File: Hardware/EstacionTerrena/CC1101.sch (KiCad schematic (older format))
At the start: 19 parts, among them U4 CC1101RGP, U5 0915BM15A0001E, Y2 26 MHz

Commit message: Corrección de librerías en PCB de estación terrena
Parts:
- removed U4: CC1101RGP, SamacSys_Parts:QFN50P400X400X100-21N-D, symbol EstacionTerrena-rescue:CC1101RGP-SamacSys_Parts
- removed U5: 0915BM15A0001E, SamacSys_Parts:0915BM15A0001E, symbol EstacionTerrena-rescue:0915BM15A0001E-SamacSys_Parts
- added U4: CC1101RGP, QFN50P400X400X100-21N-D, symbol SamacSys_Parts:CC1101RGP
- added U5: 0915BM15A0001E, 0915BM15A0001E, symbol SamacSys_Parts:0915BM15A0001E
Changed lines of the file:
@@
 EESchema Schematic File Version 4
 LIBS:EstacionTerrena-cache
-EELAYER 26 0
+EELAYER 29 0
 EELAYER END
 $Descr A4 11693 8268
@@
 	0    -1   -1   0
 $EndComp
-$Comp
-L EstacionTerrena-rescue:0915BM15A0001E-SamacSys_Parts U5
-U 1 1 5BF115E1
-P 7150 3400
-F 0 "U5" H 7150 3766 50  0000 C CNN
-F 1 "0915BM15A0001E" H 7150 3674 50  0000 C CNN
-F 2 "SamacSys_Parts:0915BM15A0001E" H 7500 3600 50  0001 L CNN
-F 3 "http://www.mouser.com/datasheet/2/611/0915BM15A0001-242333.pdf" H 7500 3500 50  0001 L CNN
-F 4 "Signal Conditioning 915MHz BALUN/FILTER" H 7500 3400 50  0001 L CNN "Description"
-F 5 "0.8" H 7500 3300 50  0001 L CNN "Height"
-F 6 "JOHANSON TECHNOLOGY" H 7500 3200 50  0001 L CNN "Manufacturer_Name"
-F 7 "0915BM15A0001E" H 7500 3100 50  0001 L CNN "Manufacturer Part Number"
-F 8 "0915BM15A0001E" H 7500 3000 50  0001 L CNN "Arrow Part Number"
-	1    7150 3400
-	1    0    0    -1
-$EndComp
 Wire Wire Line
 	6400 3300 6650 3300
@@
 Wire Wire Line
 	2900 2300 3500 2300
-$Comp
-L EstacionTerrena-rescue:CC1101RGP-SamacSys_Parts U4
-U 1 1 5BBFFFB0
-P 2900 3150
-F 0 "U4" H 4200 3800 50  0000 L CNN
-F 1 "CC1101RGP" H 4200 3700 50  0000 L CNN
-F 2 "SamacSys_Parts:QFN50P400X400X100-21N-D" H 4250 3650 50  0001 L CNN
-F 3 "http://www.ti.com/lit/ds/symlink/cc1101.pdf" H 4250 3550 50  0001 L CNN
-F 4 "Texas Instruments CC1101RGP, RF Transceiver IC Triple Band 1.8  3.6 V 20-Pin QFN" H 4250 3450 50  0001 L CNN "Description"
-F 5 "1" H 4250 3350 50  0001 L CNN "Height"
-F 6 "Texas Instruments" H 4250 3250 50  0001 L CNN "Manufacturer_Name"
-F 7 "CC1101RGP" H 4250 3150 50  0001 L CNN "Manufacturer Part Number"
-F 8 "8203068P" H 4250 3050 50  0001 L CNN "RS Part Number"
-F 9 "http://uk.rs-online.com/web/p/products/8203068P" H 4250 2950 50  0001 L CNN "RS Price/Stock"
-F 10 "CC1101RGP" H 4250 2850 50  0001 L CNN "Arrow Part Number"
-F 11 "https://www.arrow.com/en/products/cc1101rgp/texas-instruments" H 4250 2750 50  0001 L CNN "Arrow Price/Stock"
-	1    2900 3150
-	1    0    0    -1
-$EndComp
 Text HLabel 3150 4700 0    50   Input ~ 0
 CS
@@
 F 6 "GCM155R71C104KA55D" H 4500 3750 50  0001 C CNN "Manufacturer Part Number"
 	1    4500 3750
-	-1   0    0    -1
+	1    0    0    -1
 $EndComp
 $Comp
@@
 EndData
 $EndBitmap
+$Comp
+L SamacSys_Parts:CC1101RGP U4
+U 1 1 5CD02CD0
+P 2900 3150
+F 0 "U4" H 4000 3850 50  0000 L CNN
+F 1 "CC1101RGP" H 4000 3750 50  0000 L CNN
+F 2 "QFN50P400X400X100-21N-D" H 4250 3650 50  0001 L CNN
+F 3 "http://www.ti.com/lit/ds/symlink/cc1101.pdf" H 4250 3550 50  0001 L CNN
+F 4 "Texas Instruments CC1101RGP, RF Transceiver IC Triple Band 1.8  3.6 V 20-Pin QFN" H 4250 3450 50  0001 L CNN "Description"
+F 5 "1" H 4250 3350 50  0001 L CNN "Height"
+F 6 "Texas Instruments" H 4250 3250 50  0001 L CNN "Manufacturer_Name"
+F 7 "CC1101RGP" H 4250 3150 50  0001 L CNN "Manufacturer Part Number"
+F 8 "8203068P" H 4250 3050 50  0001 L CNN "RS Part Number"
+F 9 "http://uk.rs-online.com/web/p/products/8203068P" H 4250 2950 50  0001 L CNN "RS Price/Stock"
+F 10 "CC1101RGP" H 4250 2850 50  0001 L CNN "Arrow Part Number"
+F 11 "https://www.arrow.com/en/products/cc1101rgp/texas-instruments" H 4250 2750 50  0001 L CNN "Arrow Price/Stock"
+	1    2900 3150
+	1    0    0    -1
+$EndComp
+$Comp
+L SamacSys_Parts:0915BM15A0001E U5
+U 1 1 5CD0A297
+P 7150 3400
+F 0 "U5" H 7150 3765 50  0000 C CNN
+F 1 "0915BM15A0001E" H 7150 3674 50  0000 C CNN
+F 2 "0915BM15A0001E" H 7500 3600 50  0001 L CNN
+F 3 "http://www.mouser.com/datasheet/2/611/0915BM15A0001-242333.pdf" H 7500 3500 50  0001 L CNN
+F 4 "Signal Conditioning 915MHz BALUN/FILTER" H 7500 3400 50  0001 L CNN "Description"
+F 5 "0.8" H 7500 3300 50  0001 L CNN "Height"
+F 6 "JOHANSON TECHNOLOGY" H 7500 3200 50  0001 L CNN "Manufacturer_Name"
+F 7 "0915BM15A0001E" H 7500 3100 50  0001 L CNN "Manufacturer Part Number"
+F 8 "0915BM15A0001E" H 7500 3000 50  0001 L CNN "Arrow Part Number"
+	1    7150 3400
+	1    0    0    -1
+$EndComp
 $EndSCHEMATC

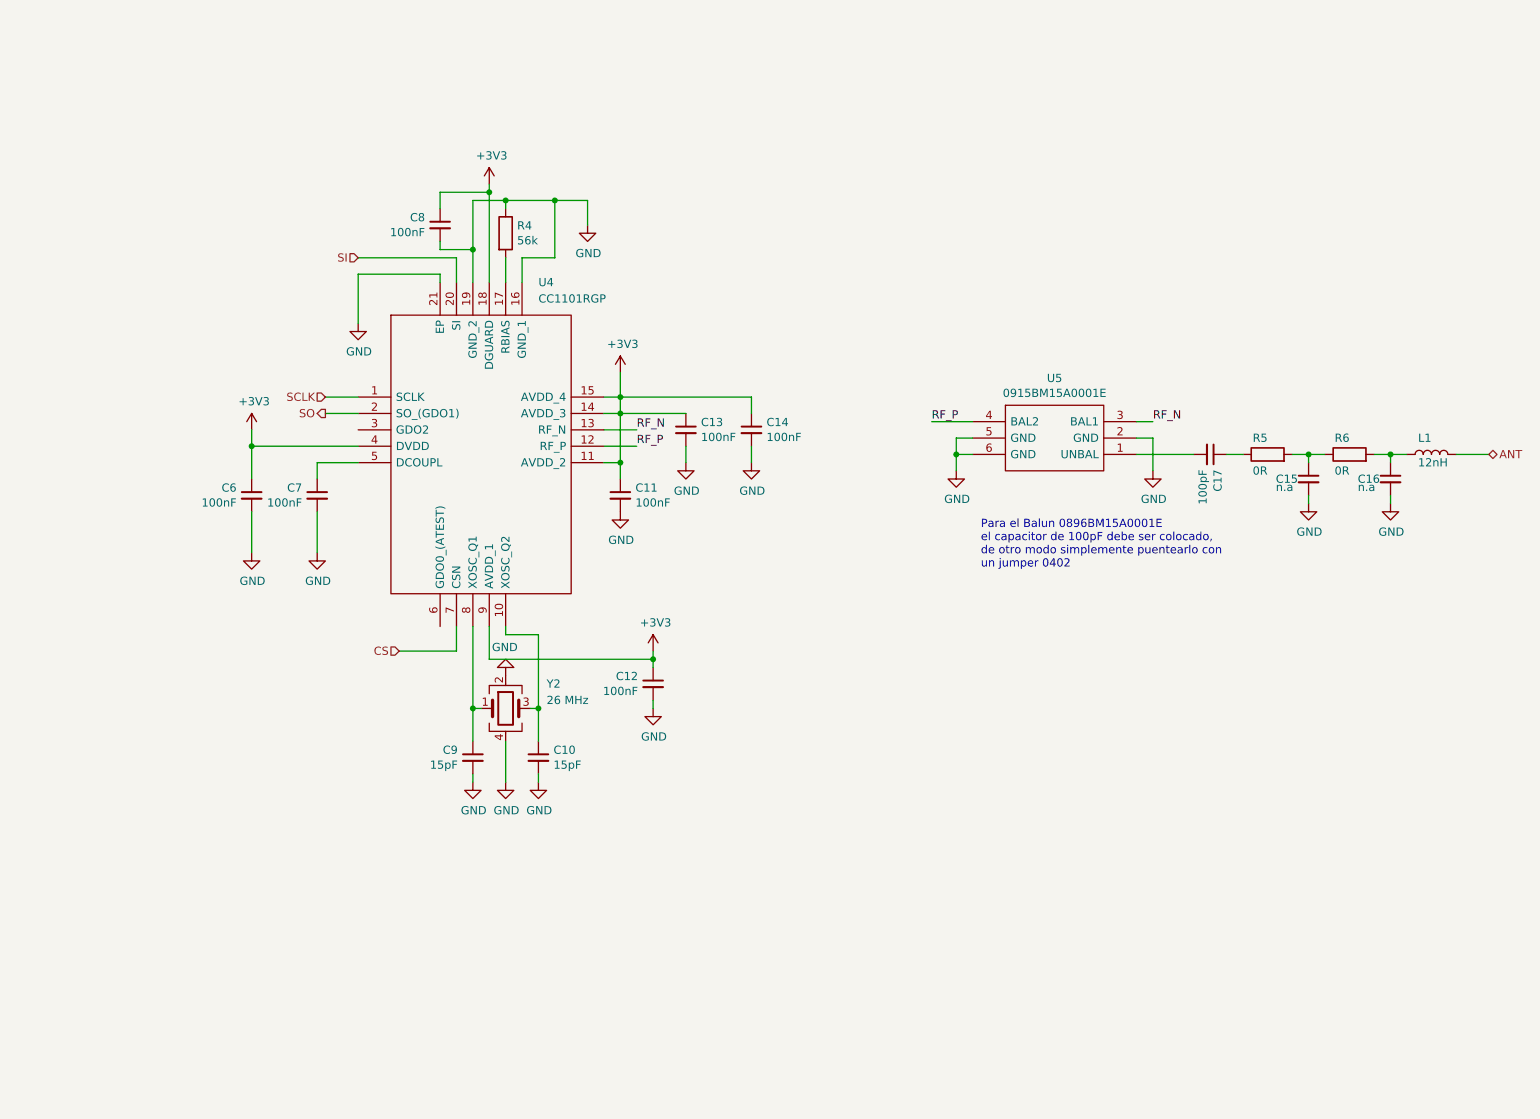
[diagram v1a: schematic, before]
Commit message: Agregado CC1190 a estación terrena
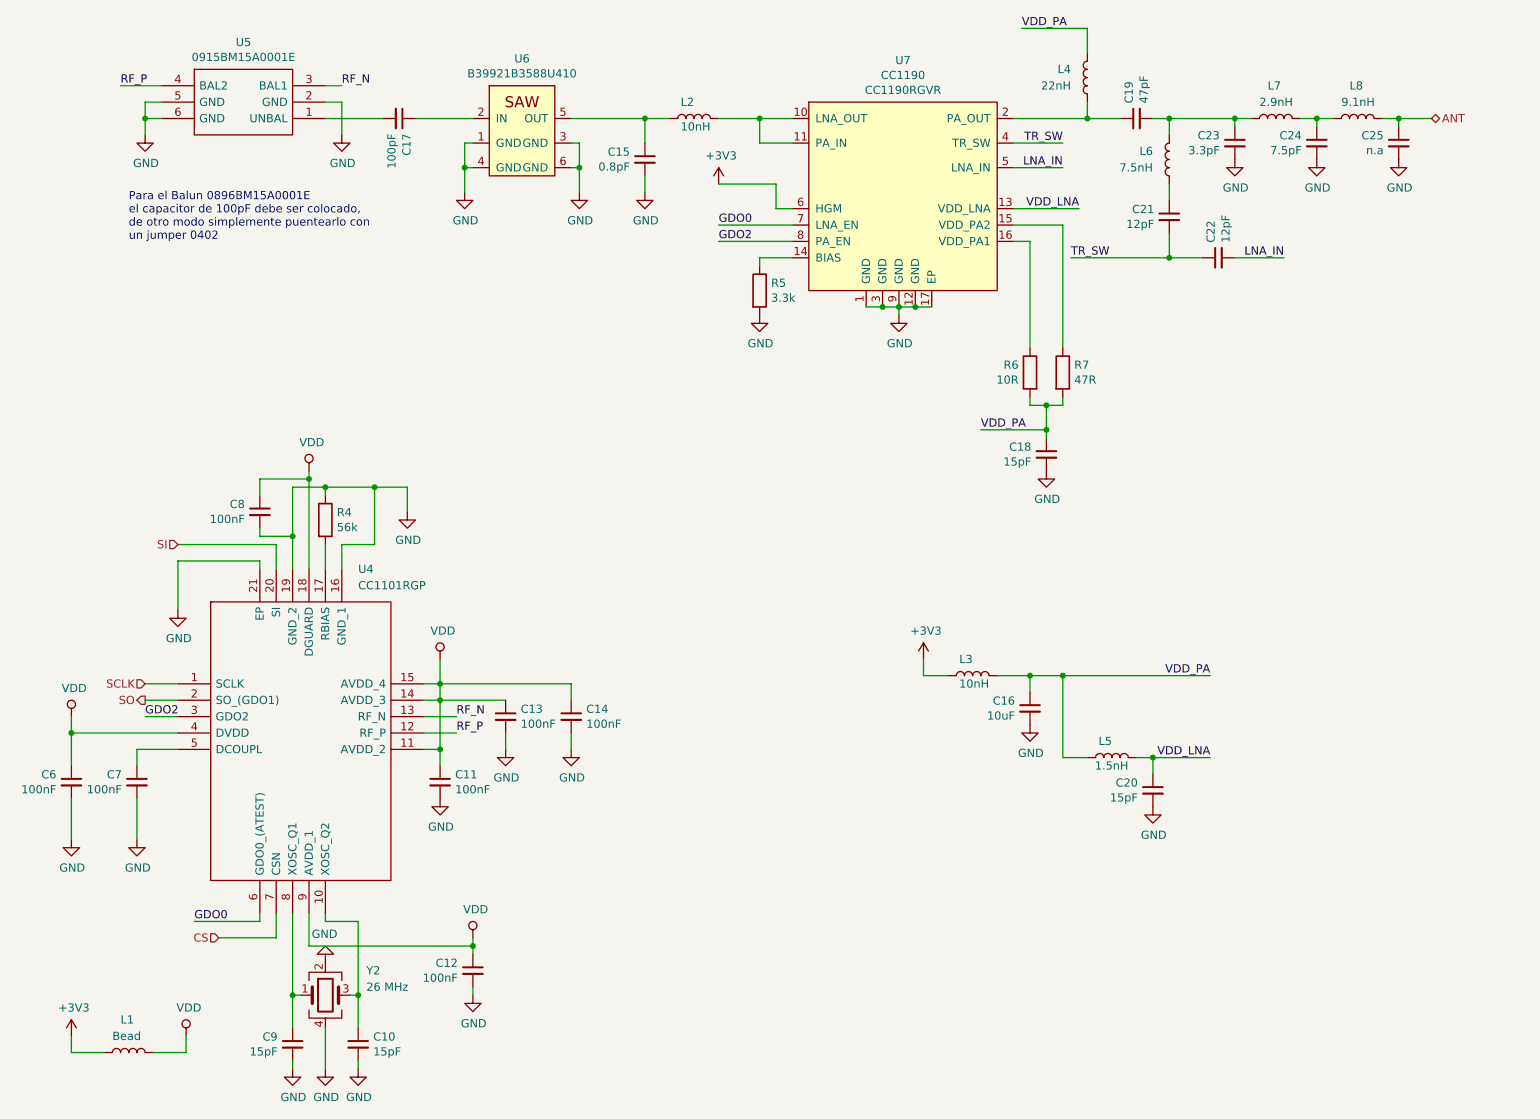
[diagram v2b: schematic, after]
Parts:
- added C18, C20: 15pF, Capacitor_SMD:C_0402_1005Metric, symbol Device:C_Small
- added C19: 47pF, Capacitor_SMD:C_0402_1005Metric, symbol Device:C_Small
- added C21, C22: 12pF, Capacitor_SMD:C_0402_1005Metric, symbol Device:C_Small
- added C23: 3.3pF, Capacitor_SMD:C_0402_1005Metric, symbol Device:C_Small
- added C24: 7.5pF, Capacitor_SMD:C_0402_1005Metric, symbol Device:C_Small
- added C25: n.a, Capacitor_SMD:C_0402_1005Metric, symbol Device:C_Small
- added L2, L3: 10nH, Inductor_SMD:L_0402_1005Metric, symbol Device:L
- added L4: 22nH, Inductor_SMD:L_0603_1608Metric_Pad1.05x0.95mm_HandSolder, symbol Device:L
- added L5: 1.5nH, Inductor_SMD:L_0402_1005Metric, symbol Device:L
- added L6: 7.5nH, Inductor_SMD:L_0402_1005Metric, symbol Device:L
- added L7: 2.9nH, Inductor_SMD:L_0402_1005Metric, symbol Device:L
- added L8: 9.1nH, Inductor_SMD:L_0402_1005Metric, symbol Device:L
- added R7: 47R, Resistor_SMD:R_0402_1005Metric, symbol Device:R
- added U6: B39921B3588U410, AXTEC:B39921B3588U410, symbol AXTEC_IC:B39921B3588U410
- added U7: CC1190, Package_DFN_QFN:Texas_S-PVQFN-N16_EP2.7x2.7mm, symbol AXTEC_IC:CC1190
- C15: value n.a -> 0.8pF; Dielectric (none) -> NP0; Manufacturer Part Number (none) -> GRM1555C2AR80BA01D
- C16: value n.a -> 10uF; footprint Capacitor_SMD:C_0402_1005Metric -> Capacitor_SMD:C_0805_2012Metric_Pad1.15x1.40mm_HandSolder; Dielectric (none) -> NP0; Manufacturer Part Number (none) -> C2012X7R1A106M125AC
- L1: value 12nH -> Bead; Manufacturer Part Number L-07C12NJV6 -> BLM15HG102SN1D
- R5: value 0R -> 3.3k; Manufacturer Part Number RC0402JR-070RL -> RC0402FR-073K3L
- R6: value 0R -> 10R; Manufacturer Part Number RC0402JR-070RL -> RC0402FR-0710RL
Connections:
- net +3V3: now also L1.2, L3.1, U7.6 (HGM); no longer C11.1, C12.1, C13.1, C14.1, C6.1, C8.1, U4.11 (AVDD_2), U4.14 (AVDD_3), U4.15 (AVDD_4), U4.18 (DGUARD), U4.4 (DVDD), U4.9 (AVDD_1)
- net ANT: now also C25.1, L8.1; no longer L1.2
- net GND: now also R5.2, C18.2, C20.2, C23.2, C24.2, C25.2, U6.1 (GND), U6.3 (GND), U6.4 (GND), U6.6 (GND), U7.1 (GND), U7.12 (GND), U7.17 (EP), U7.3 (GND), U7.9 (GND)
- net at C17.1: now also U6.2 (IN); no longer R5.1
- net VDD_PA: now reaches C16.1, R6.2
- net VDD_PA: now also C18.1, L3.2, L4.1, L5.1, R7.2; no longer L1.1
- net GDO2: now reaches U4.3 (GDO2)
- net GDO2: now also U7.8 (PA_EN)
- net GDO0: now reaches U4.6 (GDO0_(ATEST))
- net GDO0: now also U7.7 (LNA_EN)
- new net: C15.1, L2.1, U6.5 (OUT)
- new net: L2.2, U7.10 (LNA_OUT), U7.11 (PA_IN)
- new net: C19.1, L4.2, U7.2 (PA_OUT)
- new net: C19.2, C23.1, L6.1, L7.2
- new net: C21.1, L6.2
- new net: C24.1, L7.1, L8.2
- new net: R5.1, U7.14 (BIAS)
- new net: R7.1, U7.15 (VDD_PA2)
- new net: R6.1, U7.16 (VDD_PA1)
- new net LNA_IN: C22.2, U7.5 (LNA_IN)
- new net TR_SW: C21.2, C22.1, U7.4 (TR_SW)
- new net VDD: C11.1, C12.1, C13.1, C14.1, C6.1, C8.1, L1.1, U4.11 (AVDD_2), U4.14 (AVDD_3), U4.15 (AVDD_4), U4.18 (DGUARD), U4.4 (DVDD), U4.9 (AVDD_1)
- new net VDD_LNA: C20.1, L5.2, U7.13 (VDD_LNA)
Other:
- moved on the sheet: C10, C11, C12, C13, C14, C17, C6, C7, C8, C9, R4, U4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

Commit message: Estacion terrena:
- Nuevo LDO de 500mA para poder utilizar el CC1190 a toda su potencia de ser necesario
- Cambiado el MCP2210 por un PIC18F14K50 ya que el MCP2210 es MUY lento para transferencias SPI
- Agregado de footprints faltantes
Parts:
- U4: footprint QFN50P400X400X100-21N-D -> Package_DFN_QFN:QFN-20-1EP_4x4mm_P0.5mm_EP2.5x2.5mm
- U5: footprint 0915BM15A0001E -> SamacSys_Parts:0915BM15A0001E
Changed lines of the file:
@@
 F 0 "U4" H 2900 5600 50  0000 L CNN
 F 1 "CC1101RGP" H 2900 5500 50  0000 L CNN
-F 2 "QFN50P400X400X100-21N-D" H 3150 5400 50  0001 L CNN
+F 2 "Package_DFN_QFN:QFN-20-1EP_4x4mm_P0.5mm_EP2.5x2.5mm" H 3150 5400 50  0001 L CNN
 F 3 "http://www.ti.com/lit/ds/symlink/cc1101.pdf" H 3150 5300 50  0001 L CNN
 F 4 "Texas Instruments CC1101RGP, RF Transceiver IC Triple Band 1.8  3.6 V 20-Pin QFN" H 3150 5200 50  0001 L CNN "Description"
@@
 F 0 "U5" H 2200 1715 50  0000 C CNN
 F 1 "0915BM15A0001E" H 2200 1624 50  0000 C CNN
-F 2 "0915BM15A0001E" H 2550 1550 50  0001 L CNN
+F 2 "SamacSys_Parts:0915BM15A0001E" H 2550 1550 50  0001 L CNN
 F 3 "http://www.mouser.com/datasheet/2/611/0915BM15A0001-242333.pdf" H 2550 1450 50  0001 L CNN
 F 4 "Signal Conditioning 915MHz BALUN/FILTER" H 2550 1350 50  0001 L CNN "Description"

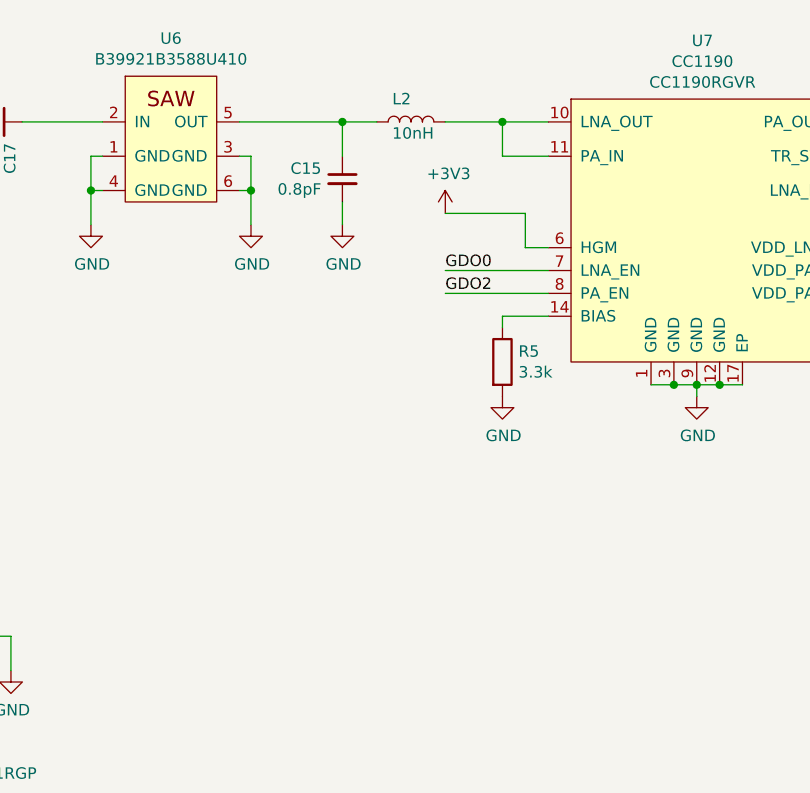
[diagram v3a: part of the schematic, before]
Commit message: Agregado jumper de selección de ganancia para CC1190 en ET
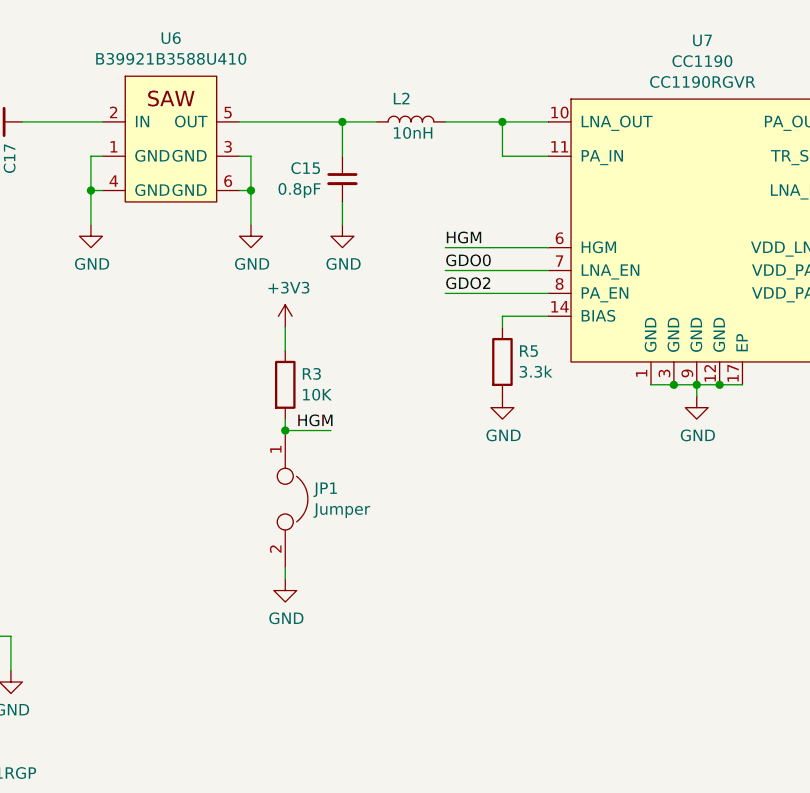
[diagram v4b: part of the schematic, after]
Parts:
- added JP1: Jumper, Jumper:SolderJumper-2_P1.3mm_Open_RoundedPad1.0x1.5mm, symbol Device:Jumper
- added R3: 10K, Resistor_SMD:R_0603_1608Metric_Pad1.05x0.95mm_HandSolder, symbol Device:R
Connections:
- net +3V3: now also R3.1; no longer U7.6 (HGM)
- net GND: now also JP1.2
- new net HGM: JP1.1, R3.2, U7.6 (HGM)
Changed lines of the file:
@@
 	5550 2100 5100 2100
-Wire Wire Line
-	5100 1850 5450 1850
-Wire Wire Line
-	5450 2000 5450 1850
-Wire Wire Line
-	5550 2000 5450 2000
 Wire Wire Line
 	5350 1450 5550 1450
@@
 RF_N
 $Comp
-L power:+3V3 #PWR033
-U 1 1 5CCF98DA
-P 5100 1850
-F 0 "#PWR033" H 5100 1700 50  0001 C CNN
-F 1 "+3V3" H 5115 2023 50  0000 C CNN
-F 2 "" H 5100 1850 50  0001 C CNN
-F 3 "" H 5100 1850 50  0001 C CNN
-	1    5100 1850
-	1    0    0    -1
-$EndComp
-$Comp
 L power:+3V3 #PWR049
 U 1 1 5CCFCB92
@@
 	1    0    0    -1
 $EndComp
+$Comp
+L power:GND #PWR016
+U 1 1 5CD4AF72
+P 4400 3450
+AR Path="/5B9A8077/5CD4AF72" Ref="#PWR016"  Part="1"
+AR Path="/5BA17F9C/5CD4AF72" Ref="#PWR?"  Part="1"
+F 0 "#PWR016" H 4400 3200 50  0001 C CNN
+F 1 "GND" H 4405 3277 50  0000 C CNN
+F 2 "" H 4400 3450 50  0001 C CNN
+F 3 "" H 4400 3450 50  0001 C CNN
+	1    4400 3450
+	1    0    0    -1
+$EndComp
+$Comp
+L Device:R R3
+U 1 1 5CD6637D
+P 4400 2600
+AR Path="/5B9A8077/5CD6637D" Ref="R3"  Part="1"
+AR Path="/5BA17F9C/5CD6637D" Ref="R?"  Part="1"
+F 0 "R3" H 4470 2646 50  0000 L CNN
+F 1 "10K" H 4470 2555 50  0000 L CNN
+F 2 "Resistor_SMD:R_0603_1608Metric_Pad1.05x0.95mm_HandSolder" V 4330 2600 50  0001 C CNN
+F 3 "~" H 4400 2600 50  0001 C CNN
+F 4 "RC0603JR-0710KL" H 4400 2600 50  0001 C CNN "Manufacturer Part Number"
+	1    4400 2600
+	1    0    0    -1
+$EndComp
+Wire Wire Line
+	5550 2000 5100 2000
+Text Label 5100 2000 0    50   ~ 0
+HGM
+Text Label 4450 2800 0    50   ~ 0
+HGM
+$Comp
+L power:+3V3 #PWR015
+U 1 1 5CDA2E4F
+P 4400 2350
+F 0 "#PWR015" H 4400 2200 50  0001 C CNN
+F 1 "+3V3" H 4415 2523 50  0000 C CNN
+F 2 "" H 4400 2350 50  0001 C CNN
+F 3 "" H 4400 2350 50  0001 C CNN
+	1    4400 2350
+	1    0    0    -1
+$EndComp
+Wire Wire Line
+	4400 2350 4400 2450
+$Comp
+L Device:Jumper JP1
+U 1 1 5CD5F03C
+P 4400 3100
+F 0 "JP1" V 4354 3227 50  0000 L CNN
+F 1 "Jumper" V 4445 3227 50  0000 L CNN
+F 2 "Jumper:SolderJumper-2_P1.3mm_Open_RoundedPad1.0x1.5mm" H 4400 3100 50  0001 C CNN
+F 3 "~" H 4400 3100 50  0001 C CNN
+	1    4400 3100
+	0    1    1    0
+$EndComp
+Wire Wire Line
+	4400 2750 4400 2800
+Wire Wire Line
+	4400 3400 4400 3450
+Wire Wire Line
+	4400 2800 4600 2800
+Connection ~ 4400 2800
 $EndSCHEMATC

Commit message: Estación terrena BOM
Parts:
- U7: Manufactuer Part Number CC1190RGVR -> (none); Manufacturer Part Number (none) -> CC1190RGVR
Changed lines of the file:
@@
 F 2 "Package_DFN_QFN:Texas_S-PVQFN-N16_EP2.7x2.7mm" H 6200 1950 50  0001 C CNN
 F 3 "" H 6050 1500 50  0001 C CNN
-F 4 "CC1190RGVR" H 6225 1723 50  0000 C CNN "Manufactuer Part Number"
+F 4 "CC1190RGVR" H 6225 1723 50  0000 C CNN "Manufacturer Part Number"
 	1    6050 1500
 	1    0    0    -1
